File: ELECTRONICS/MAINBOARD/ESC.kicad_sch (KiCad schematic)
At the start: 5 parts, among them J20 Conn_02x05_Odd_Even, J4 Conn_01x02_Socket, U7 STM32G031C_4-6-8_Tx

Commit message: almost done
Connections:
- net AMT_X_L: no longer U7.28 (PA8)
- net BRAKE: now also U7.40 (PD2); no longer U7.39 (PD1)
- net DACOUT1: now also U7.38 (PD0); no longer U7.41 (PD3)
- net DACOUT1_R: now also U7.16 (PA5); no longer U7.17 (PA6)
- net DACOUT2: now also U7.37 (PA15); no longer U7.40 (PD2)
- net DACOUT2/SOX: now also U7.39 (PD1)
- net DACOUT2_R: now also U7.15 (PA4); no longer U7.16 (PA5)
- net DACOUT2/SOX_R: now also U7.17 (PA6)
- net DIR: now also U7.41 (PD3); no longer U7.44 (PB5)
- net DRVOFF: now also U7.3 (PC15); no longer U7.43 (PB4)
- net EXT_WD: now also U7.42 (PB3); no longer U7.38 (PD0)
- net FG: now also U7.47 (PB8); no longer U7.46 (PB7)
- net PWM: now also U7.48 (PB9); no longer U7.45 (PB6)
- net PWM_R: now also U7.33 (PA9/PA11); no longer U7.15 (PA4)
- net SCL: now also U7.45 (PB6); no longer U7.47 (PB8)
- net SDA: now also U7.46 (PB7); no longer U7.48 (PB9)
- net nFAULT: now also U7.44 (PB5); no longer U7.42 (PB3)
- net nFAULT_R: now also U7.14 (PA3); no longer U7.23 (PB11)
- new net AMT_X_R: U7.28 (PA8)
- no-connect marks 6 -> 5
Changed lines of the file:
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@@
 		(at 77.47 116.84)
 	)
-	(no_connect
-		(at 114.3 86.36)
-	)
 	(wire
 		(pts
@@
 	(wire
 		(pts
+			(xy 149.86 55.88) (xy 162.56 55.88)
+		)
+		(stroke
+			(width 0)
+			(type default)
+		)
+	)
+	(wire
+		(pts
 			(xy 203.2 102.87) (xy 220.98 102.87)
 		)
@@
 	(wire
 		(pts
-			(xy 149.86 63.5) (xy 162.56 63.5)
+			(xy 149.86 60.96) (xy 162.56 60.96)
 		)
 		(stroke
@@
 	(wire
 		(pts
+			(xy 104.14 86.36) (xy 114.3 86.36)
+		)
+		(stroke
+			(width 0)
+			(type default)
+		)
+	)
+	(wire
+		(pts
 			(xy 149.86 88.9) (xy 160.02 88.9)
 		)
@@
 	(wire
 		(pts
+			(xy 149.86 63.5) (xy 166.37 63.5)
+		)
+		(stroke
+			(width 0)
+			(type default)
+		)
+	)
+	(wire
+		(pts
 			(xy 219.71 26.67) (xy 220.98 26.67)
 		)
@@
 	(wire
 		(pts
-			(xy 149.86 58.42) (xy 158.75 58.42)
-		)
-		(stroke
-			(width 0)
-			(type default)
-		)
-	)
-	(wire
-		(pts
 			(xy 149.86 104.14) (xy 158.75 104.14)
 		)
@@
 	(wire
 		(pts
+			(xy 149.86 81.28) (xy 160.02 81.28)
+		)
+		(stroke
+			(width 0)
+			(type default)
+		)
+	)
+	(wire
+		(pts
 			(xy 102.87 68.58) (xy 114.3 68.58)
 		)
@@
 	(wire
 		(pts
-			(xy 102.87 66.04) (xy 114.3 66.04)
+			(xy 96.52 66.04) (xy 114.3 66.04)
 		)
 		(stroke
@@
 	(wire
 		(pts
-			(xy 149.86 60.96) (xy 162.56 60.96)
+			(xy 149.86 58.42) (xy 162.56 58.42)
 		)
 		(stroke
@@
 		)
 	)
-	(label "DRVOFF"
-		(at 158.75 96.52 180)
-		(effects
-			(font
-				(size 1.27 1.27)
-			)
-			(justify right bottom)
-		)
-	)
-	(label "FG"
+	(label "PWM"
+		(at 158.75 109.22 180)
+		(effects
+			(font
+				(size 1.27 1.27)
+			)
+			(justify right bottom)
+		)
+	)
+	(label "SDA"
 		(at 158.75 104.14 180)
 		(effects
@@
 		)
 	)
-	(label "DACOUT1"
-		(at 102.87 71.12 0)
-		(effects
-			(font
-				(size 1.27 1.27)
-			)
-			(justify left bottom)
-		)
-	)
 	(label "EXT_WD_R"
 		(at 220.98 115.57 180)
@@
 	)
 	(label "BRAKE"
-		(at 102.87 66.04 0)
-		(effects
-			(font
-				(size 1.27 1.27)
-			)
-			(justify left bottom)
+		(at 102.87 68.58 0)
+		(effects
+			(font
+				(size 1.27 1.27)
+			)
+			(justify left bottom)
+		)
+	)
+	(label "nFAULT"
+		(at 158.75 99.06 180)
+		(effects
+			(font
+				(size 1.27 1.27)
+			)
+			(justify right bottom)
 		)
 	)
@@
 		)
 	)
+	(label "nFAULT_R"
+		(at 162.56 55.88 180)
+		(effects
+			(font
+				(size 1.27 1.27)
+			)
+			(justify right bottom)
+		)
+	)
 	(label "FG_R"
 		(at 171.45 104.14 0)
@@
 		)
 	)
+	(label "PWM_R"
+		(at 160.02 71.12 180)
+		(effects
+			(font
+				(size 1.27 1.27)
+			)
+			(justify right bottom)
+		)
+	)
+	(label "DACOUT1"
+		(at 102.87 63.5 0)
+		(effects
+			(font
+				(size 1.27 1.27)
+			)
+			(justify left bottom)
+		)
+	)
 	(label "DACOUT1_R"
-		(at 162.56 63.5 180)
+		(at 162.56 60.96 180)
 		(effects
 			(font
@@
 		)
 	)
+	(label "SCL"
+		(at 158.75 101.6 180)
+		(effects
+			(font
+				(size 1.27 1.27)
+			)
+			(justify right bottom)
+		)
+	)
 	(label "DRVOFF"
 		(at 218.44 74.93 180)
@@
 		)
 	)
+	(label "DRVOFF"
+		(at 104.14 86.36 0)
+		(effects
+			(font
+				(size 1.27 1.27)
+			)
+			(justify left bottom)
+		)
+	)
 	(label "VREF"
 		(at 107.95 48.26 0)
@@
 		)
 	)
-	(label "PWM"
-		(at 158.75 101.6 180)
-		(effects
-			(font
-				(size 1.27 1.27)
-			)
-			(justify right bottom)
-		)
-	)
 	(label "SWDIO"
 		(at 85.09 109.22 180)
@@
 		)
 	)
+	(label "EXT_WD"
+		(at 158.75 93.98 180)
+		(effects
+			(font
+				(size 1.27 1.27)
+			)
+			(justify right bottom)
+		)
+	)
 	(label "DIR_R"
 		(at 171.45 101.6 0)
@@
 	)
 	(label "DACOUT2"
-		(at 102.87 68.58 0)
-		(effects
-			(font
-				(size 1.27 1.27)
-			)
-			(justify left bottom)
+		(at 160.02 81.28 180)
+		(effects
+			(font
+				(size 1.27 1.27)
+			)
+			(justify right bottom)
 		)
 	)
@@
 		)
 	)
+	(label "FG"
+		(at 158.75 106.68 180)
+		(effects
+			(font
+				(size 1.27 1.27)
+			)
+			(justify right bottom)
+		)
+	)
 	(label "BRAKE_R"
 		(at 220.98 102.87 180)
@@
 		)
 	)
-	(label "SDA"
-		(at 158.75 109.22 180)
-		(effects
-			(font
-				(size 1.27 1.27)
-			)
-			(justify right bottom)
-		)
-	)
 	(label "USART_TX"
 		(at 88.9 83.82 180)
@@
 		)
 	)
+	(label "DACOUT2{slash}SOX_R"
+		(at 166.37 63.5 180)
+		(effects
+			(font
+				(size 1.27 1.27)
+			)
+			(justify right bottom)
+		)
+	)
 	(label "DIR"
-		(at 158.75 99.06 180)
-		(effects
-			(font
-				(size 1.27 1.27)
-			)
-			(justify right bottom)
+		(at 102.87 71.12 0)
+		(effects
+			(font
+				(size 1.27 1.27)
+			)
+			(justify left bottom)
 		)
 	)
@@
 		)
 	)
+	(label "DACOUT2/SOX"
+		(at 96.52 66.04 0)
+		(effects
+			(font
+				(size 1.27 1.27)
+			)
+			(justify left bottom)
+		)
+	)
 	(label "FG_R"
 		(at 158.75 124.46 180)
@@
 		)
 	)
-	(label "nFAULT"
-		(at 158.75 93.98 180)
-		(effects
-			(font
-				(size 1.27 1.27)
-			)
-			(justify right bottom)
-		)
-	)
 	(label "SWCLK"
 		(at 160.02 78.74 180)
@@
 		)
 	)
-	(label "EXT_WD"
-		(at 102.87 63.5 0)
-		(effects
-			(font
-				(size 1.27 1.27)
-			)
-			(justify left bottom)
-		)
-	)
 	(label "USART_TX"
 		(at 104.14 93.98 0)
@@
 		)
 	)
-	(label "SCL"
-		(at 158.75 106.68 180)
-		(effects
-			(font
-				(size 1.27 1.27)
-			)
-			(justify right bottom)
-		)
-	)
 	(label "EXT_WD_R"
 		(at 160.02 88.9 180)
@@
 		)
 	)
-	(label "PWM_R"
-		(at 158.75 58.42 180)
-		(effects
-			(font
-				(size 1.27 1.27)
-			)
-			(justify right bottom)
-		)
-	)
 	(label "SCL_R"
 		(at 158.75 119.38 180)
@@
 	)
 	(label "DACOUT2_R"
-		(at 162.56 60.96 180)
+		(at 162.56 58.42 180)
 		(effects
 			(font
@@
 	(label "SWCLK"
 		(at 85.09 106.68 180)
-		(effects
-			(font
-				(size 1.27 1.27)
-			)
-			(justify right bottom)
-		)
-	)
-	(label "nFAULT_R"
-		(at 158.75 114.3 180)
 		(effects
 			(font
@@
 		)
 	)
-	(hierarchical_label "AMT_X_L"
+	(hierarchical_label "AMT_X_R"
 		(shape input)
 		(at 149.86 68.58 0)

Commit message: add mosfets
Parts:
- J4: footprint (none) -> Connector_JST:JST_PH_B2B-PH-K_1x02_P2.00mm_Vertical
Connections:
- net USART_RX: now also J4.2 (Pin_2); no longer J4.1 (Pin_1)
- net USART_TX: now also J4.1 (Pin_1); no longer J4.2 (Pin_2)
- net AMTGATE_R: now reaches U7.23 (PB11)
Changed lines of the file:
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@@
 	(wire
 		(pts
-			(xy 149.86 114.3) (xy 158.75 114.3)
+			(xy 149.86 114.3) (xy 152.4 114.3)
 		)
 		(stroke
@@
 	)
 	(label "USART_RX"
-		(at 88.9 95.25 180)
+		(at 88.9 83.82 180)
 		(effects
 			(font
@@
 	)
 	(label "USART_TX"
-		(at 88.9 83.82 180)
+		(at 88.9 95.25 180)
 		(effects
 			(font
@@
 	(hierarchical_label "USART_RX"
 		(shape input)
-		(at 78.74 90.17 0)
+		(at 78.74 87.63 0)
 		(effects
 			(font
@@
 	(hierarchical_label "USART_TX"
 		(shape output)
-		(at 78.74 87.63 0)
+		(at 78.74 90.17 0)
 		(effects
 			(font
@@
 		)
 	)
+	(hierarchical_label "AMTGATE_R"
+		(shape output)
+		(at 152.4 114.3 0)
+		(effects
+			(font
+				(size 1.27 1.27)
+			)
+			(justify left)
+		)
+	)
 	(hierarchical_label "3V3"
 		(shape input)
@@
 			)
 			(justify right)
+		)
+	)
+	(hierarchical_label "AMTGATE_2"
+		(shape output)
+		(at 57.15 66.04 0)
+		(effects
+			(font
+				(size 1.27 1.27)
+			)
+			(justify left)
 		)
 	)
@@
 			)
 		)
-		(property "Footprint" ""
+		(property "Footprint" "Connector_JST:JST_PH_B2B-PH-K_1x02_P2.00mm_Vertical"
 			(at 67.31 90.17 0)
 			(hide yes)

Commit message: change tvs
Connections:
- net AMTGATE_2: now also U7.1 (PC13)
- no-connect marks 5 -> 4
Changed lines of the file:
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@@
-	)
-	(no_connect
-		(at 114.3 81.28)
 	)
 	(no_connect
@@
 		(pts
 			(xy 102.87 68.58) (xy 114.3 68.58)
+		)
+		(stroke
+			(width 0)
+			(type default)
+		)
+	)
+	(wire
+		(pts
+			(xy 111.76 81.28) (xy 114.3 81.28)
 		)
 		(stroke
@@
 	(hierarchical_label "AMTGATE_2"
 		(shape output)
-		(at 57.15 66.04 0)
-		(effects
-			(font
-				(size 1.27 1.27)
-			)
-			(justify left)
-		)
-	)
+		(at 111.76 81.28 180)
+		(effects
+			(font
+				(size 1.27 1.27)
+			)
+			(justify right)
+		)
+	)

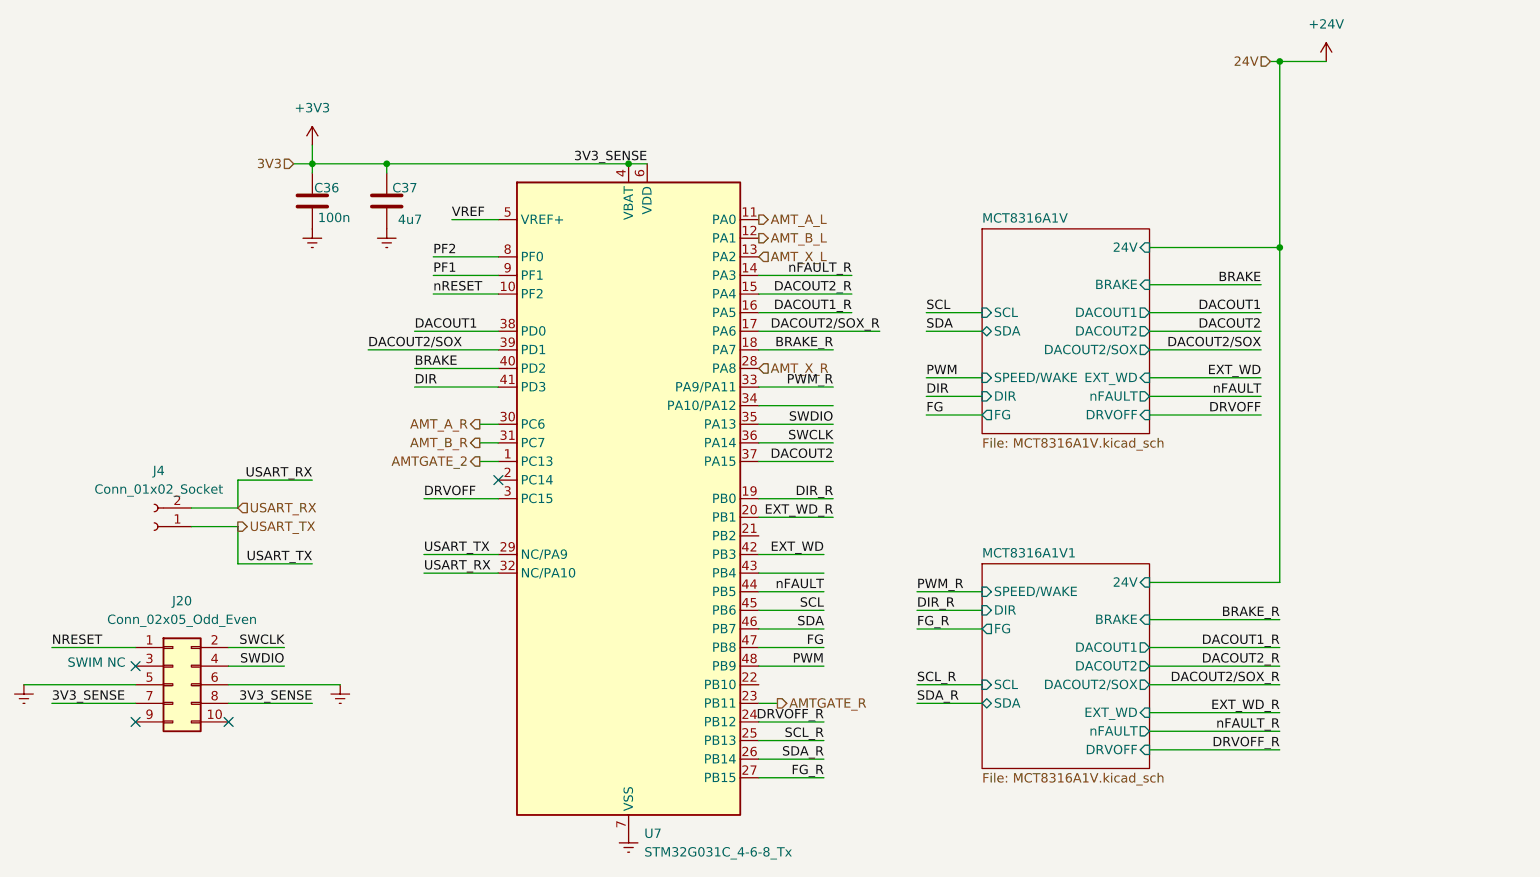
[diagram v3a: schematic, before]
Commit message: change tvs1400 to another tvs with higher clamping voltage. fix footprints and add nreset
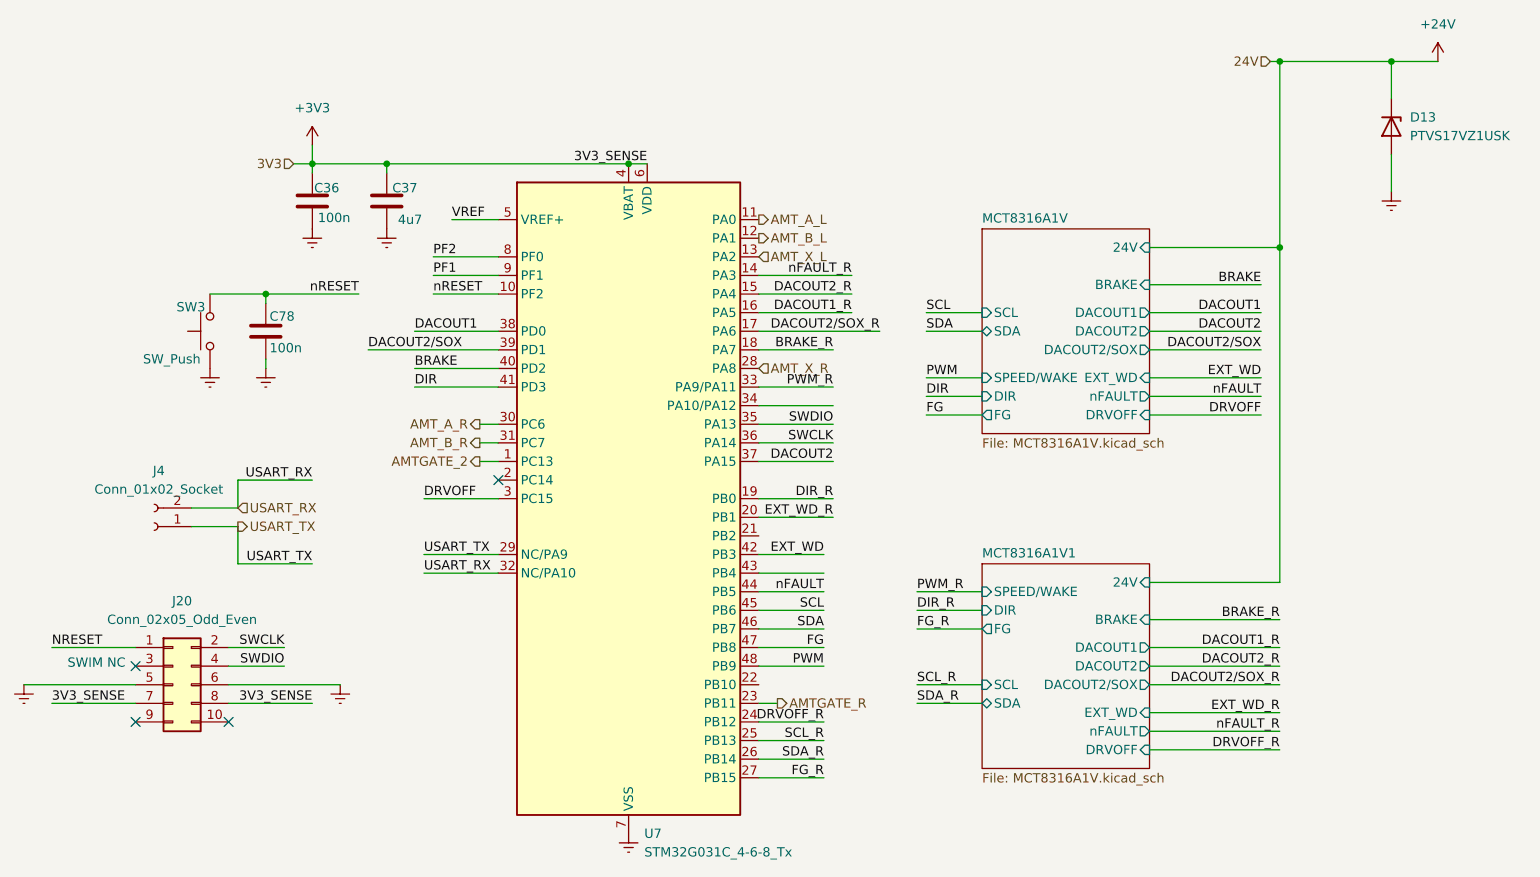
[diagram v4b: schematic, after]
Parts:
- added C78: 100n, Capacitor_SMD:C_0402_1005Metric, symbol Device:C
- added D13: PTVS17VZ1USK, Diode_SMD:Nexperia_CFP3_SOD-123W, symbol Diode:PTVS15VZ1USK
- added SW3: SW_Push, Button_Switch_THT:SW_PUSH_6mm, symbol Switch:SW_Push
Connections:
- net +24V: now also D13.1 (K)
- net GNDREF: now also C78.2, D13.2 (A), SW3.1
- net nRESET: now also C78.1, SW3.2

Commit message: functionally finished driver board
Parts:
- added TP1, TP2, TP3, TP4: TestPoint, symbol Connector:TestPoint
- SW3: footprint Button_Switch_THT:SW_PUSH_6mm -> MyFootprintLibrary:SW-SMD_L3.9-W3.0-P4.45
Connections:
- net +24V: now also TP1.1
- net +3V3: now also TP4.1
- net GNDREF: now also TP2.1
- net nRESET: now also TP3.1
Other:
- note added: "note: pa14 is also boot0"

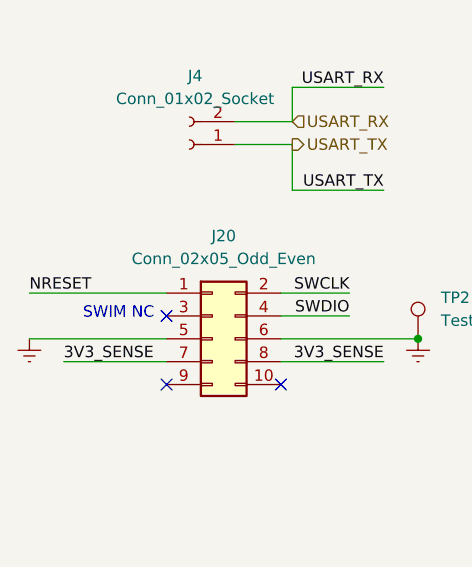
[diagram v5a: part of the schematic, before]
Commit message: resize driver board to 60x55 mm^2, spread out bldc motor out pads
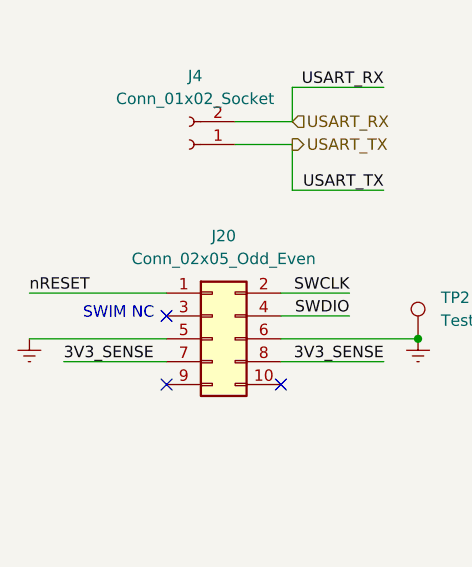
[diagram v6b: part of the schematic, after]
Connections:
- net NRESET is gone; now on net nRESET: J20.1 (Pin_1)
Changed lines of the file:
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@@
 		)
 	)
-	(label "NRESET"
+	(label "nRESET"
 		(at 49.53 106.68 0)
 		(effects
